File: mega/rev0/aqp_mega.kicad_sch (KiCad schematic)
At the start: 173 parts, among them J1 Power in, J10 FPGA spare, J11 Hand controller 2, J12 Hand controller 1, J13 ESP32 spare, J2 ESP USB Host, J3 Audio out, J4 VGA, J5 Cassette out, J6 Cassette in, J7 Expansion port, J8 Printer, J9 TF-03A, Q1 BC847C, Q2 BC847C, Q3 2N7002, SW1 SW_DPDT_x2, U1 SN74AHCT1G125DBVR, U10 ESP32-S3-WROOM-1-N4R2, U11 LDL1117S33R, U12 SN74CB3T3245PWR, U13 IS61C5128AS-25QLI, U2 SN74AHCT1G125DBVR, U3 LD1117S12, U4 SN74CB3T3245PWR, U5 MAX3221ECPWR, U6 XC6SLX9-2TQG144C, U7 Z84C3008VEG, U8 SN74CB3T3245PWR, U9 SN74CB3T3245PWR, X1 SX3M14.31818M20F30TNN

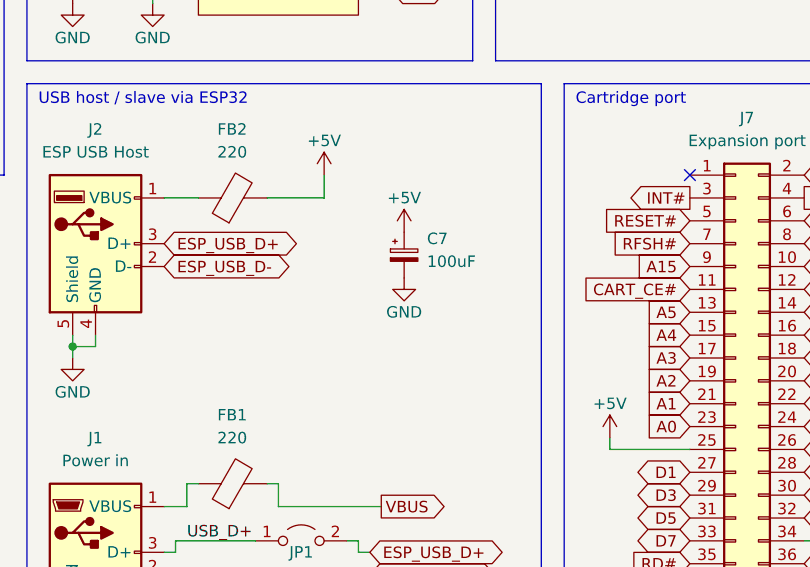
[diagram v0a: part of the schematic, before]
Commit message: PCB folder updates and reorg
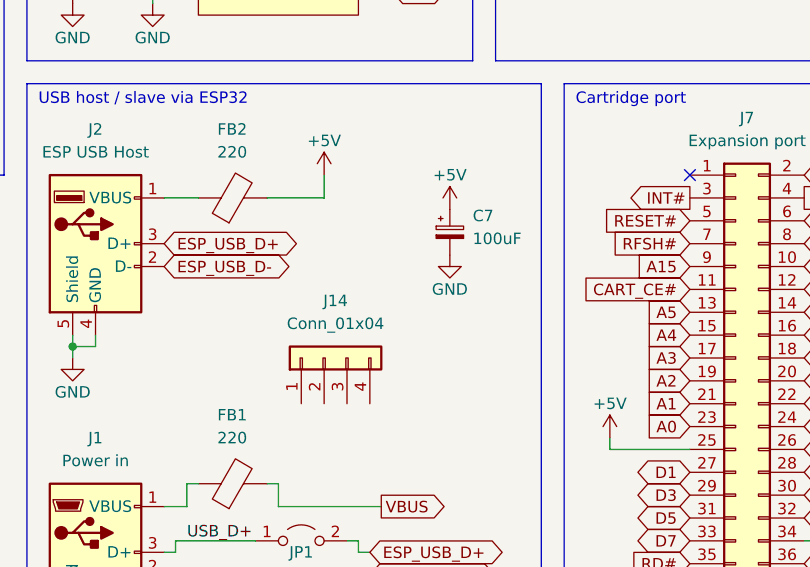
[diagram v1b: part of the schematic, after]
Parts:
- added J14: Conn_01x04, Connector_PinHeader_2.54mm:PinHeader_1x04_P2.54mm_Vertical, symbol Connector_Generic:Conn_01x04
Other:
- moved on the sheet: C7
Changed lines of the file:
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@@
 	(symbol
 		(lib_id "power:GND")
-		(at 281.94 115.57 0)
+		(at 287.02 113.03 0)
 		(unit 1)
 		(exclude_from_sim no)
@@
 		(dnp no)
 		(property "Reference" "#PWR0131"
-			(at 281.94 121.92 0)
+			(at 287.02 119.38 0)
 			(effects
 				(font
@@
 		)
 		(property "Value" "GND"
-			(at 281.94 119.38 0)
+			(at 287.02 116.84 0)
 			(effects
 				(font
@@
 		)
 		(property "Footprint" ""
-			(at 281.94 115.57 0)
+			(at 287.02 113.03 0)
 			(effects
 				(font
@@
 		)
 		(property "Datasheet" ""
-			(at 281.94 115.57 0)
+			(at 287.02 113.03 0)
 			(effects
 				(font
@@
 		)
 		(property "Description" ""
-			(at 281.94 115.57 0)
+			(at 287.02 113.03 0)
 			(effects
 				(font
@@
 	(symbol
 		(lib_id "Device:C_Polarized_Small")
-		(at 281.94 113.03 0)
+		(at 287.02 110.49 0)
 		(unit 1)
 		(exclude_from_sim no)
@@
 		(fields_autoplaced yes)
 		(property "Reference" "C7"
-			(at 284.48 111.2138 0)
+			(at 289.56 108.6738 0)
 			(effects
 				(font
@@
 		)
 		(property "Value" "100uF"
-			(at 284.48 113.7538 0)
+			(at 289.56 111.2138 0)
 			(effects
 				(font
@@
 		)
 		(property "Footprint" "Capacitor_SMD:CP_Elec_6.3x7.7"
-			(at 281.94 113.03 0)
+			(at 287.02 110.49 0)
 			(effects
 				(font
@@
 		)
 		(property "Datasheet" "~"
-			(at 281.94 113.03 0)
+			(at 287.02 110.49 0)
 			(effects
 				(font
@@
 		)
 		(property "Description" ""
-			(at 281.94 113.03 0)
+			(at 287.02 110.49 0)
 			(effects
 				(font
@@
 	(symbol
 		(lib_id "power:+5V")
-		(at 281.94 110.49 0)
+		(at 287.02 107.95 0)
 		(unit 1)
 		(exclude_from_sim no)
@@
 		(dnp no)
 		(property "Reference" "#PWR0130"
-			(at 281.94 114.3 0)
+			(at 287.02 111.76 0)
 			(effects
 				(font
@@
 		)
 		(property "Value" "+5V"
-			(at 281.94 106.68 0)
+			(at 287.02 104.14 0)
 			(effects
 				(font
@@
 		)
 		(property "Footprint" ""
-			(at 281.94 110.49 0)
+			(at 287.02 107.95 0)
 			(effects
 				(font
@@
 		)
 		(property "Datasheet" ""
-			(at 281.94 110.49 0)
+			(at 287.02 107.95 0)
 			(effects
 				(font
@@
 		)
 		(property "Description" ""
-			(at 281.94 110.49 0)
+			(at 287.02 107.95 0)
 			(effects
 				(font
@@
 					(unit 1)
 				)
+			)
+		)
+	)
+	(symbol
+		(lib_id "Connector_Generic:Conn_01x04")
+		(at 273.05 124.46 90)
+		(unit 1)
+		(exclude_from_sim no)
+		(in_bom yes)
+		(on_board yes)
+		(dnp no)
+		(fields_autoplaced yes)
+		(property "Reference" "J14"
+			(at 274.32 118.11 90)
+			(effects
+				(font
+					(size 1.27 1.27)
+				)
+			)
+		)
+		(property "Value" "Conn_01x04"
+			(at 274.32 120.65 90)
+			(effects
+				(font
+					(size 1.27 1.27)
+				)
+			)
+		)
+		(property "Footprint" "Connector_PinHeader_2.54mm:PinHeader_1x04_P2.54mm_Vertical"
+			(at 273.05 124.46 0)
+			(effects
+				(font
+					(size 1.27 1.27)
+				)
+				(hide yes)
+			)
+		)
+		(property "Datasheet" "~"
+			(at 273.05 124.46 0)
+			(effects
+				(font
+					(size 1.27 1.27)
+				)
+				(hide yes)
+			)
+		)
+		(property "Description" "Generic connector, single row, 01x04, script generated (kicad-library-utils/schlib/autogen/connector/)"
+			(at 273.05 124.46 0)
+			(effects
+				(font
+					(size 1.27 1.27)
+				)
+				(hide yes)
+			)
+		)
+		(pin "2"
+		)
+		(pin "4"
+		)
+		(pin "1"
+		)
+		(pin "3"
+		)
+		(instances
+			(project ""
+				(path "/e63e39d7-6ac0-4ffd-8aa3-1841a4541b55"
+					(reference "J14")
+					(unit 1)
+				)
